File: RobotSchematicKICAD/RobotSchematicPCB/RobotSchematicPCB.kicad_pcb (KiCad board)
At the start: 2 copper layers, 1 part

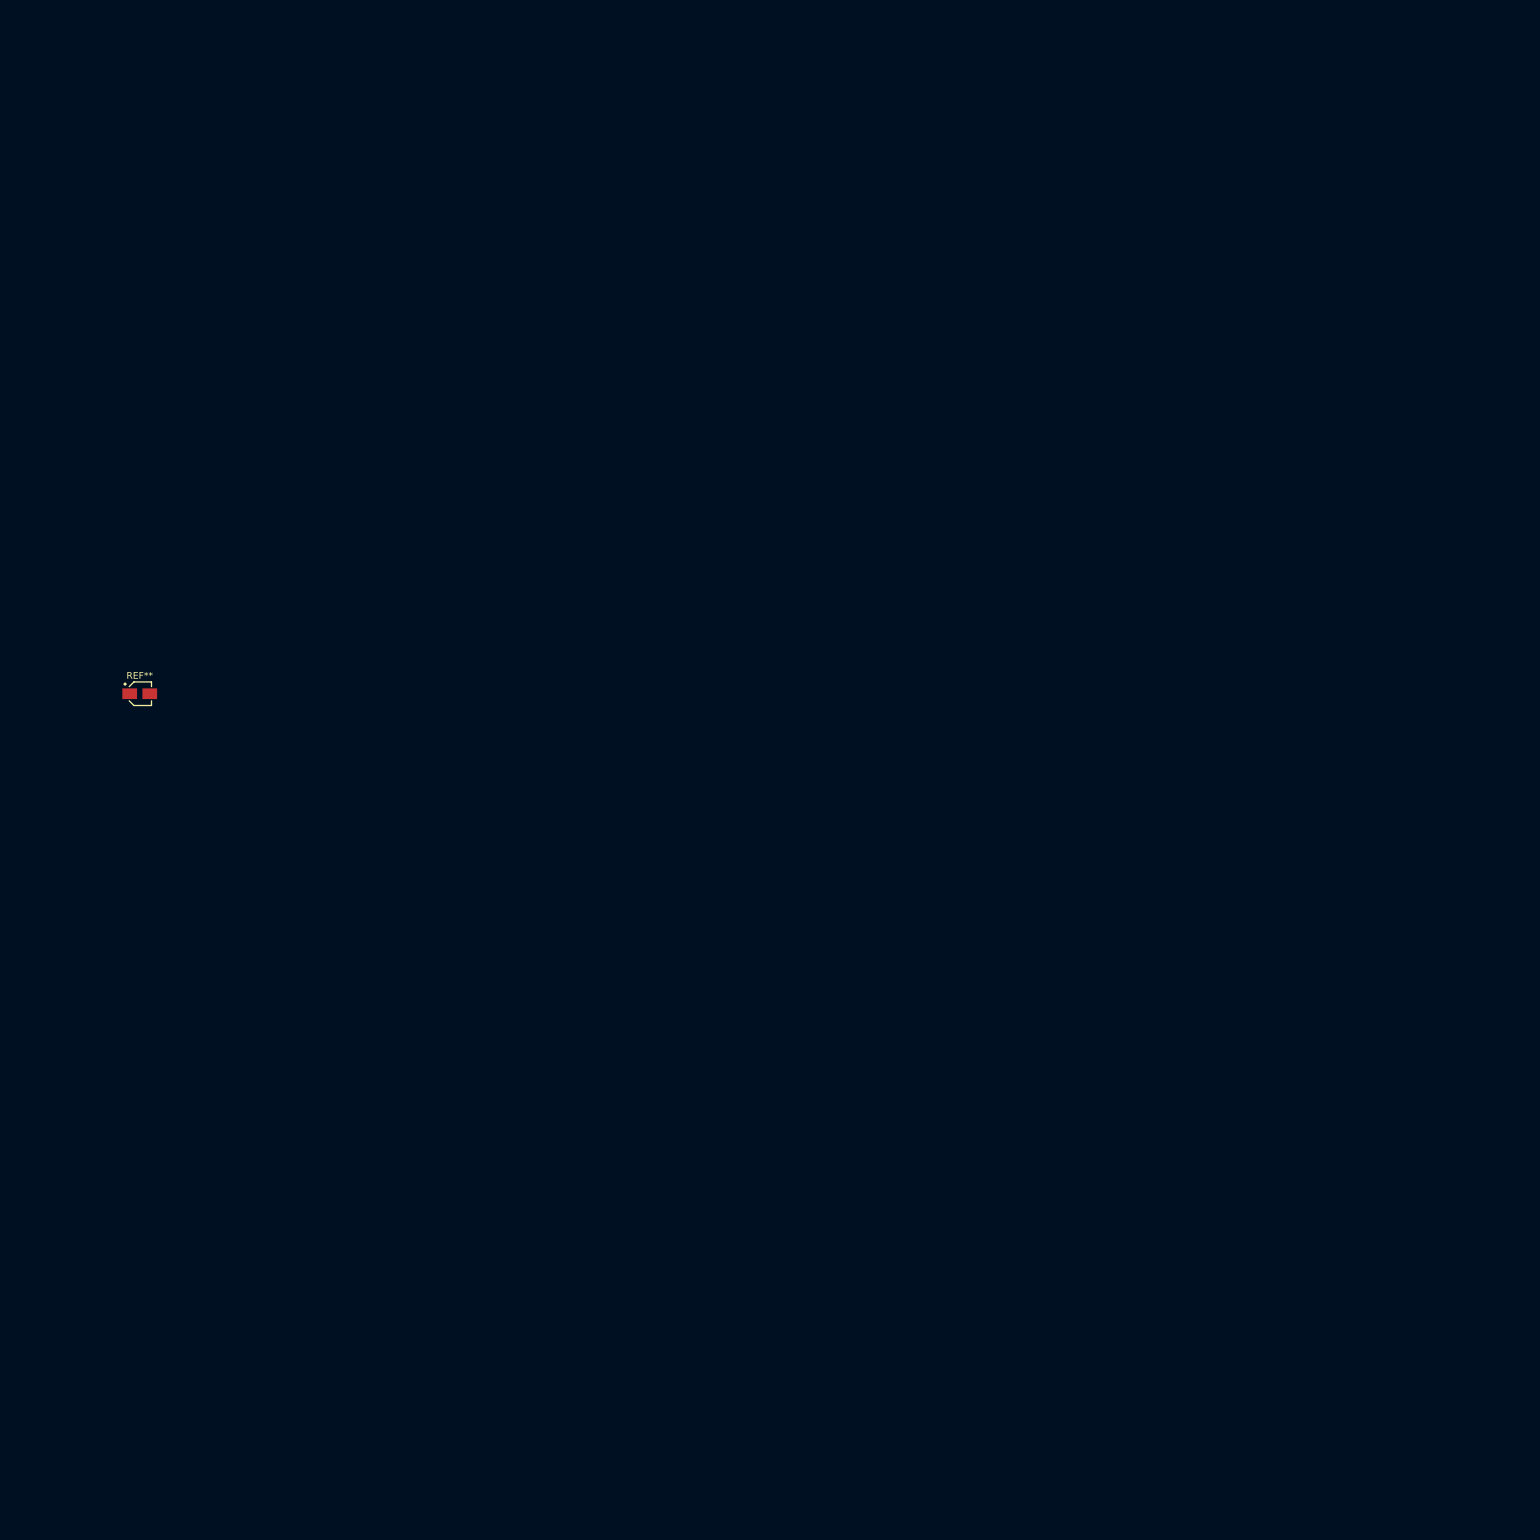
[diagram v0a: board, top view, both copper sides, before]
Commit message: imported from 3d model for exact dimensions
I imported the dxf from the model for the controller and then I made that the edge cuts for the board. I also added some art
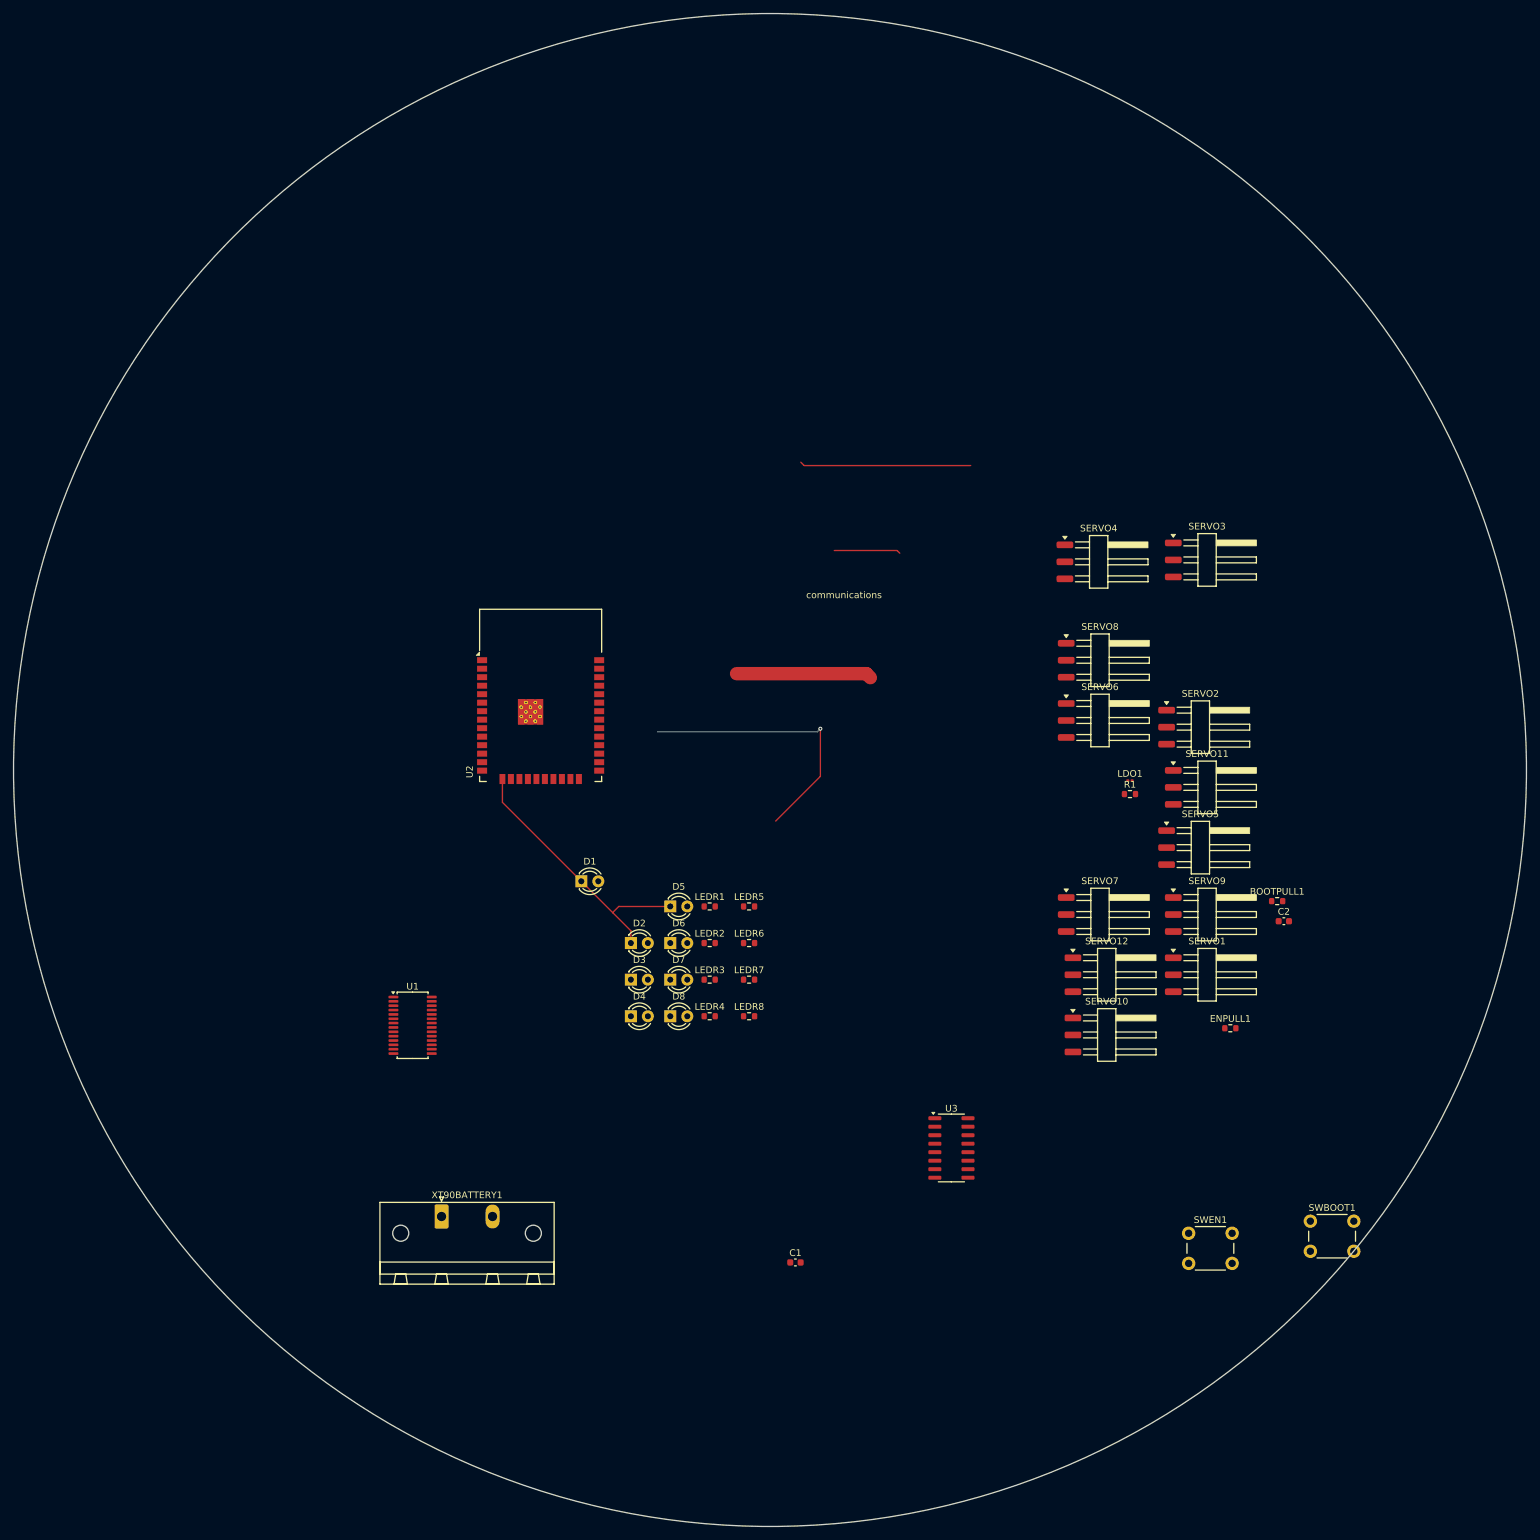
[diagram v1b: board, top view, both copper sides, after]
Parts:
- removed REF**: CP_Elec_3x5.3, Capacitor_SMD:CP_Elec_3x5.3
- added BOOTPULL1: 10k, Resistor_SMD:R_0603_1608Metric, F.Cu at (249.0, 91.0)
- added C1: 10u, Capacitor_SMD:C_0603_1608Metric, F.Cu at (177.0, 145.0)
- added C2: 10u, Capacitor_SMD:C_0603_1608Metric, F.Cu at (250.0, 94.0)
- added D1: LED, LED_THT:LED_D3.0mm, F.Cu at (145.0, 88.0)
- added D2: LED, LED_THT:LED_D3.0mm, F.Cu at (152.4, 97.3)
- added D3: LED, LED_THT:LED_D3.0mm, F.Cu at (152.4, 102.7)
- added D4: LED, LED_THT:LED_D3.0mm, F.Cu at (152.4, 108.2)
- added D5: LED, LED_THT:LED_D3.0mm, F.Cu at (158.3, 91.8)
- added D6: LED, LED_THT:LED_D3.0mm, F.Cu at (158.3, 97.3)
- added D7: LED, LED_THT:LED_D3.0mm, F.Cu at (158.3, 102.7)
- added D8: LED, LED_THT:LED_D3.0mm, F.Cu at (158.3, 108.2)
- added ENPULL1: 10k, Resistor_SMD:R_0603_1608Metric, F.Cu at (242.0, 110.0)
- added LDO1: AMS1117-3.3, Resistor_SMD:R_0201_0603Metric, F.Cu at (227.0, 73.0)
- added LEDR1: 330, Resistor_SMD:R_0603_1608Metric, F.Cu at (164.2, 91.8)
- added LEDR2: 330, Resistor_SMD:R_0603_1608Metric, F.Cu at (164.2, 97.3)
- added LEDR3: 330, Resistor_SMD:R_0603_1608Metric, F.Cu at (164.2, 102.7)
- added LEDR4: 330, Resistor_SMD:R_0603_1608Metric, F.Cu at (164.2, 108.2)
- added LEDR5: 330, Resistor_SMD:R_0603_1608Metric, F.Cu at (170.1, 91.8)
- added LEDR6: 330, Resistor_SMD:R_0603_1608Metric, F.Cu at (170.1, 97.3)
- added LEDR7: 330, Resistor_SMD:R_0603_1608Metric, F.Cu at (170.1, 102.7)
- added LEDR8: 330, Resistor_SMD:R_0603_1608Metric, F.Cu at (170.1, 108.2)
- added R1: 10k, Resistor_SMD:R_0603_1608Metric, F.Cu at (227.0, 75.0)
- added SERVO1: Conn_01x03_Pin, Connector_Harwin:Harwin_M20-89003xx_1x03_P2.54mm_Horizontal, F.Cu at (239.0, 102.0)
- added SERVO10: Conn_01x03_Pin, Connector_Harwin:Harwin_M20-89003xx_1x03_P2.54mm_Horizontal, F.Cu at (224.0, 111.0)
- added SERVO11: Conn_01x03_Pin, Connector_Harwin:Harwin_M20-89003xx_1x03_P2.54mm_Horizontal, F.Cu at (239.0, 74.0)
- added SERVO12: Conn_01x03_Pin, Connector_Harwin:Harwin_M20-89003xx_1x03_P2.54mm_Horizontal, F.Cu at (224.0, 102.0)
- added SERVO2: Conn_01x03_Pin, Connector_Harwin:Harwin_M20-89003xx_1x03_P2.54mm_Horizontal, F.Cu at (238.0, 65.0)
- added SERVO3: Conn_01x03_Pin, Connector_Harwin:Harwin_M20-89003xx_1x03_P2.54mm_Horizontal, F.Cu at (239.0, 40.0)
- added SERVO4: Conn_01x03_Pin, Connector_Harwin:Harwin_M20-89003xx_1x03_P2.54mm_Horizontal, F.Cu at (222.8, 40.3)
- added SERVO5: Conn_01x03_Pin, Connector_Harwin:Harwin_M20-89003xx_1x03_P2.54mm_Horizontal, F.Cu at (238.0, 83.0)
- added SERVO6: Conn_01x03_Pin, Connector_Harwin:Harwin_M20-89003xx_1x03_P2.54mm_Horizontal, F.Cu at (223.0, 64.0)
- added SERVO7: Conn_01x03_Pin, Connector_Harwin:Harwin_M20-89003xx_1x03_P2.54mm_Horizontal, F.Cu at (223.0, 93.0)
- added SERVO8: Conn_01x03_Pin, Connector_Harwin:Harwin_M20-89003xx_1x03_P2.54mm_Horizontal, F.Cu at (223.0, 55.0)
- added SERVO9: Conn_01x03_Pin, Connector_Harwin:Harwin_M20-89003xx_1x03_P2.54mm_Horizontal, F.Cu at (239.0, 93.0)
- added SWBOOT1: SW_Push, Button_Switch_THT:SW_PUSH_6mm, F.Cu at (254.0, 138.8)
- added SWEN1: SW_Push, Button_Switch_THT:SW_PUSH_6mm, F.Cu at (235.8, 140.6)
- added U1: PCA9685PW, Package_SO:TSSOP-28_4.4x9.7mm_P0.65mm, F.Cu at (119.8, 109.6)
- added U2: ESP32-WROOM-32E, RF_Module:ESP32-WROOM-32D, F.Cu at (138.9, 63.2)
- added U3: 74HC595, Package_SO:SOIC-16_3.9x9.9mm_P1.27mm, F.Cu at (200.3, 127.9)
- added XT90BATTERY1: Screw_Terminal_01x02, Connector_Phoenix_GMSTB:PhoenixContact_GMSTB_2,5_2-GF-7,62_1x02_P7.62mm_Horizontal_ThreadedFlange_MountHole, F.Cu at (124.1, 138.1)
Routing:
- net (no net): track 0.00 -> 96.9 mm, vias 0 -> 1
- net GND: track 0.00 -> 41.5 mm
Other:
- board outline added: 226.1 x 226.1 mm
- board text added: "communications"
